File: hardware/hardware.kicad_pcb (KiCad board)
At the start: 2 copper layers, 85.8 x 41.5 mm, 44 parts, among them J1 USB_C_Receptacle_USB2.0_16P, J2 Conn_01x02_Pin, J3 C-OBD-II-16M, J4 Conn_01x06, J5 Conn_01x02_Pin, J6 Conn_01x06, SW3 Reset, SW4 Boot, U1 ESP32-S3-WROOM-1U-N16R8, U2 MCP2515-xSO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

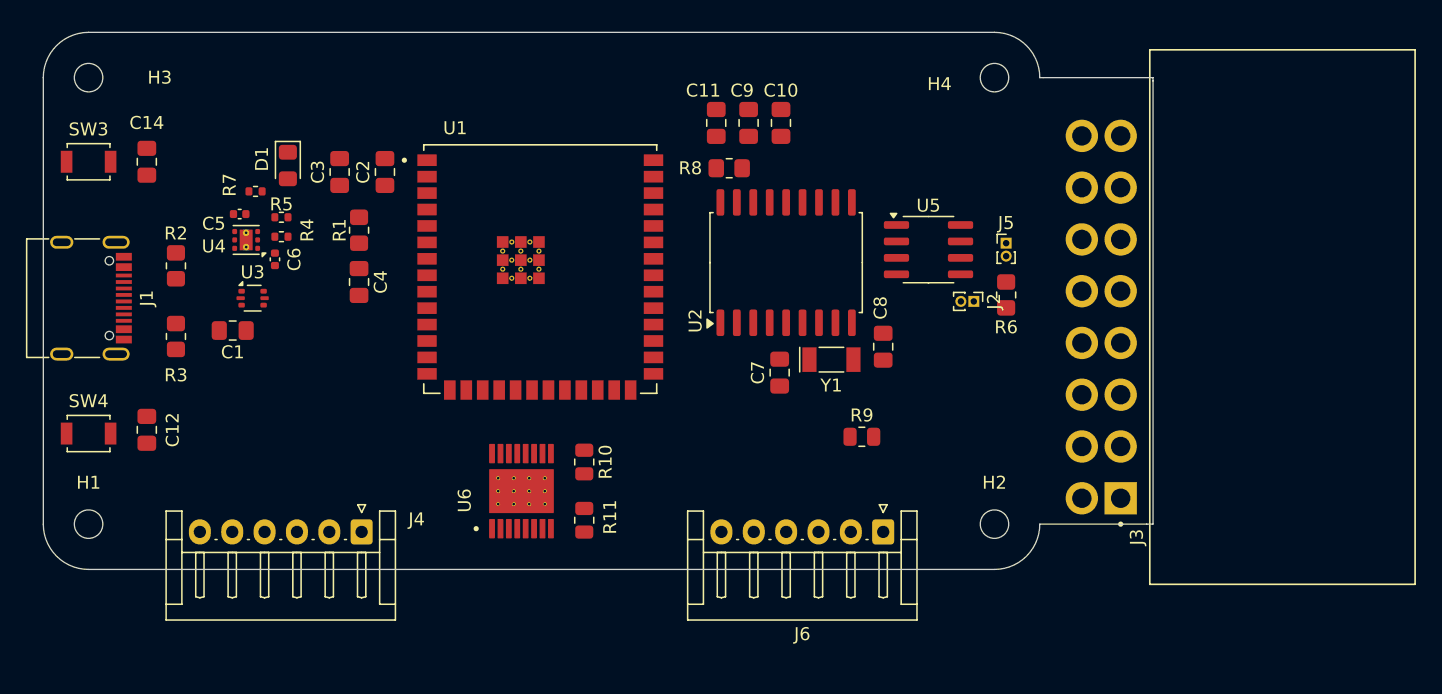
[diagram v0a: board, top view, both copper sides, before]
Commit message: Motor driver and connector
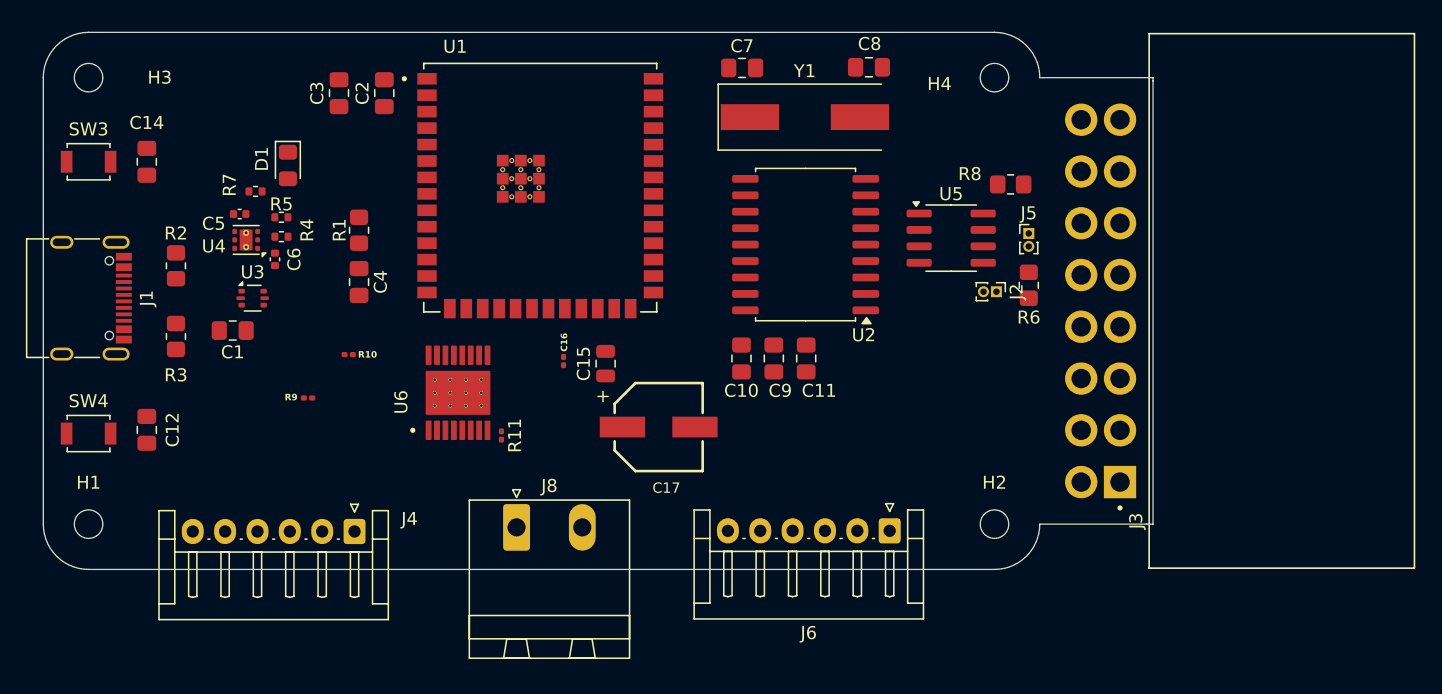
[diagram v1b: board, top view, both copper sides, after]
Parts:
- added C15: 1uF/50V, Capacitor_SMD:C_0805_2012Metric, F.Cu at (90.0, 64.1)
- added C16: 0.1uF, Capacitor_SMD:C_0201_0603Metric, F.Cu at (86.7, 63.9)
- added C17: 47uF/50V, WCAP-ASLI_6.3X7.7:WCAP-ASLI_6.3X7.7_DXL_, F.Cu at (94.0, 69.0)
- added J8: Screw_Terminal_01x02, Connector_Phoenix_MSTB:PhoenixContact_MSTBA_2,5_2-G-5,08_1x02_P5.08mm_Horizontal, F.Cu at (83.1, 76.8)
- R10, R11, R9: footprint Resistor_SMD:R_0805_2012Metric -> Resistor_SMD:R_0201_0603Metric
- Y1: footprint Crystal:Crystal_SMD_MicroCrystal_CC5V-T1A-2Pin_4.1x1.5mm -> Crystal:Crystal_SMD_HC49-SD
- moved R9 42.9 mm to (67.0, 66.8), turned to 180 degrees
- moved C7 23.7 mm to (100.5, 41.2), turned to 0 degrees
- moved R8 21.8 mm to (121.2, 50.2)
- moved C8 21.6 mm to (110.3, 41.2), turned to 0 degrees
- moved R10 20.0 mm to (70.1, 63.4), turned to 0 degrees
- moved C11 19.5 mm to (105.5, 63.7), turned to -90 degrees
- moved Y1 18.9 mm to (105.3, 45.0)
- moved C10 18.5 mm to (100.5, 63.7), turned to -90 degrees
- moved C9 18.3 mm to (103.0, 63.7), turned to -90 degrees
- moved R11 9.16 mm to (81.9, 69.7), turned to -90 degrees
- moved U6 9.04 mm to (78.5, 66.3)
- moved U1 6.29 mm to (84.9, 50.5)
- moved C2 6.09 mm to (72.8, 43.2)
- moved C3 6.09 mm to (69.3, 43.2)
- moved U2 2.05 mm to (105.4, 54.9), turned to 180 degrees
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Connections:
- U1 pad 17: unconnected-(U1-IO9-Pad17) -> /PWM_A1
- U1 pad 18: unconnected-(U1-IO10-Pad18) -> /PWM_A2
- U1 pad 19: /CAN_INT -> /PWM_B1
- U1 pad 20: unconnected-(U1-IO12-Pad20) -> /PWM_B2
- U1 pad 31: unconnected-(U1-IO38-Pad31) -> /CAN_INT
- U1 pad 38: /PWM -> unconnected-(U1-IO2-Pad38)
- U6 pad 10: unconnected-(U6-BIN2-Pad10) -> /PWM_B2
- U6 pad 12: unconnected-(U6-VM-Pad12) -> /V_Motor
- U6 pad 15: unconnected-(U6-AIN2-Pad15) -> /PWM_A2
- U6 pad 16: /PWM -> /PWM_A1
- U6 pad 9: unconnected-(U6-BIN1-Pad9) -> /PWM_B1

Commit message: Added Leds and moved from 2 to 4 layers pcb
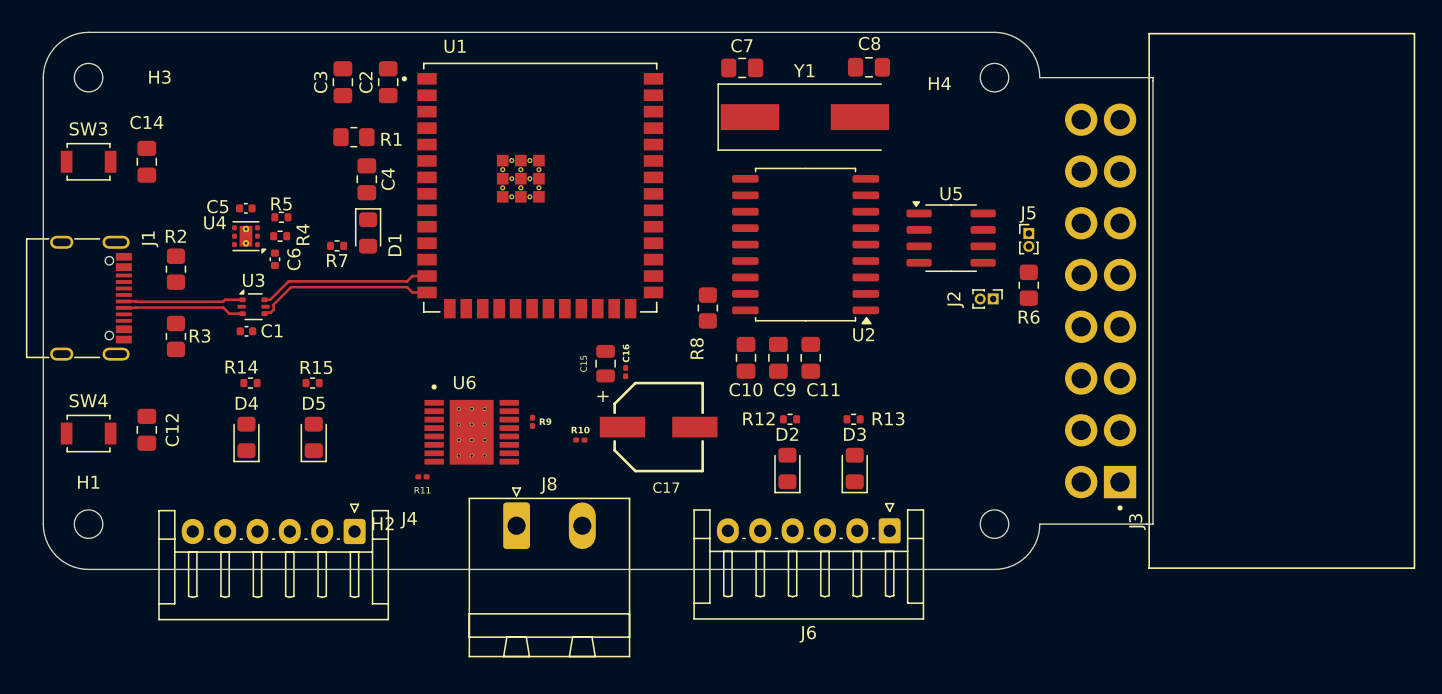
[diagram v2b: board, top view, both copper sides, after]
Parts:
- added D2: LED, LED_SMD:LED_0805_2012Metric_Pad1.15x1.40mm_HandSolder, F.Cu at (104.0, 72.2)
- added D3: LED, LED_SMD:LED_0805_2012Metric_Pad1.15x1.40mm_HandSolder, F.Cu at (109.2, 72.2)
- added D4: LED, LED_SMD:LED_0805_2012Metric_Pad1.15x1.40mm_HandSolder, F.Cu at (62.2, 69.8)
- added D5: LED, LED_SMD:LED_0805_2012Metric_Pad1.15x1.40mm_HandSolder, F.Cu at (67.4, 69.8)
- added R12: 130, Resistor_SMD:R_0402_1005Metric, F.Cu at (104.2, 68.4)
- added R13: 130, Resistor_SMD:R_0402_1005Metric, F.Cu at (109.1, 68.4)
- added R14: 130, Resistor_SMD:R_0402_1005Metric, F.Cu at (62.5, 65.6)
- added R15: 130, Resistor_SMD:R_0402_1005Metric, F.Cu at (67.3, 65.6)
- C1: footprint Capacitor_SMD:C_0805_2012Metric_Pad1.18x1.45mm_HandSolder -> Capacitor_SMD:C_0402_1005Metric
- moved R8 25.3 mm to (97.8, 59.8), turned to -90 degrees
- moved R10 19.1 mm to (88.0, 70.0)
- moved R9 17.4 mm to (84.3, 68.6), turned to -90 degrees
- moved D1 8.10 mm to (71.6, 54.0)
- moved C4 7.96 mm to (71.5, 49.9)
- moved R7 7.58 mm to (69.2, 55.0)
- moved R1 7.20 mm to (70.5, 46.6), turned to 0 degrees
- moved R11 6.89 mm to (75.8, 72.8), turned to 180 degrees
- moved C16 4.87 mm to (91.5, 64.8)
- moved U6 3.23 mm to (79.6, 69.4), turned to 0 degrees
- moved C1 1.06 mm to (62.2, 61.6)
- moved C2 0.90 mm to (73.2, 42.4)
- moved C3 0.90 mm to (69.7, 42.4)
- moved U3 0.66 mm to (62.8, 59.7)
- moved C5 0.65 mm to (62.1, 52.1)
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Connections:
- J4 pad 2: /EncoderA+ -> /3.3V
- J4 pad 5: /EncoderA- -> GND
- J6 pad 2: /EncoderB+ -> /3.3V
- J6 pad 5: /EncoderB- -> GND
- U1 pad 13: /GPIO19 -> /D-
- U1 pad 14: /GPIO20 -> /D+
- U1 pad 19: /PWM_B1 -> /PWM_B2
- U1 pad 20: /PWM_B2 -> /PWM_B1
- U1 pad 21: unconnected-(U1-IO13-Pad21) -> /PulseB_01
- U1 pad 22: /Pulse_01 -> /PulseB_02
- U1 pad 31: /CAN_INT -> /CS
- U1 pad 32: /SCLK -> /MISO
- U1 pad 34: /MISO -> /SCLK
- U1 pad 35: /CS -> /CAN_INT
- U1 pad 8: /Pulse_02 -> /PulseA_02
- U1 pad 9: unconnected-(U1-IO16-Pad9) -> /PulseA_01
- U3 pad 4: /GPIO20 -> /D+
- U3 pad 6: /GPIO19 -> /D-
- U6 pad 10: /PWM_B2 -> unconnected-(U6-BIN2-Pad10)
- U6 pad 15: /PWM_A2 -> unconnected-(U6-AIN2-Pad15)
- U6 pad 16: /PWM_A1 -> unconnected-(U6-AIN1-Pad16)
- U6 pad 9: /PWM_B1 -> unconnected-(U6-BIN1-Pad9)
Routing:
- net /D+: track 0.00 -> 23.2 mm
- net /D-: track 0.00 -> 22.6 mm
- added copper zone on In1.Cu, net GND
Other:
- copper layers 2 -> 4

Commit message: Changed motor driver IC from DRV8411 to DRV8871 PCB updated as well added manufacture values in schematics
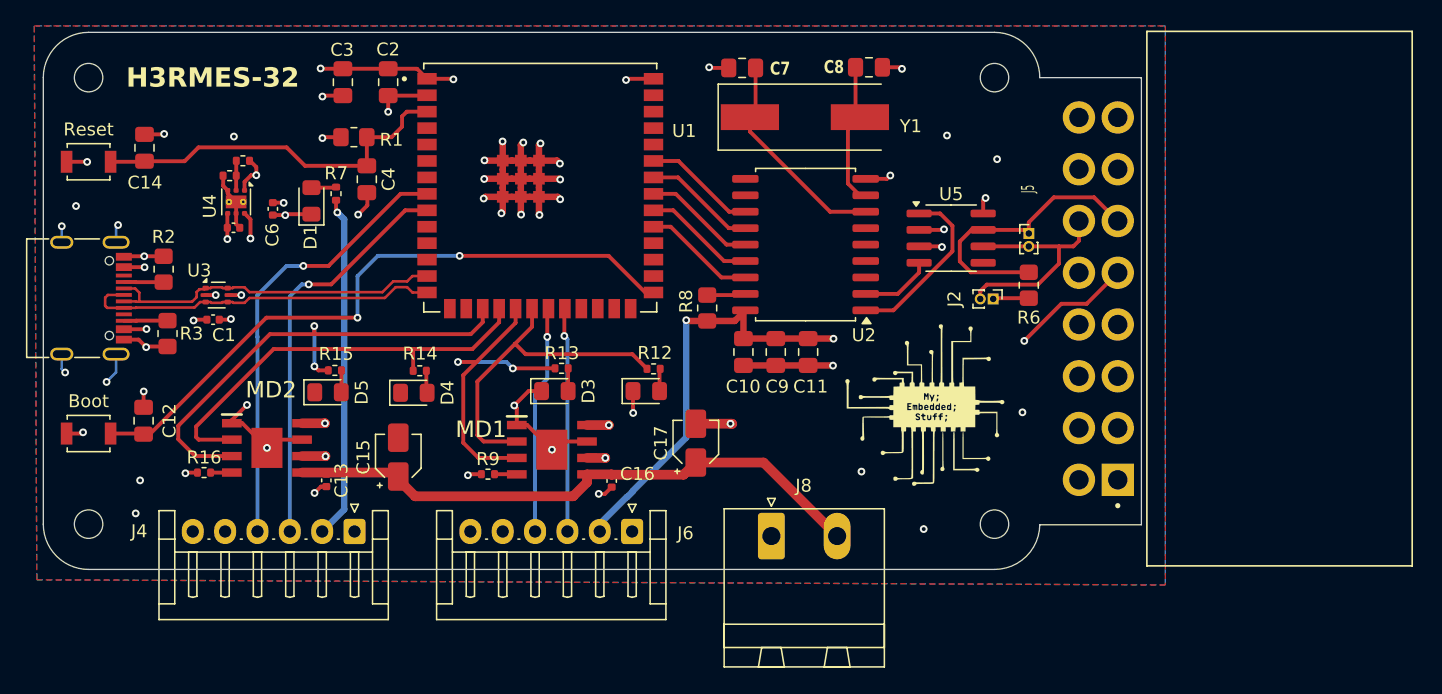
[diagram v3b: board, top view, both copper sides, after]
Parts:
- removed R10: R, Resistor_SMD:R_0201_0603Metric
- removed R11: 10K, Resistor_SMD:R_0201_0603Metric
- removed U6: DRV8411APWPR, DRV8411APWPR:IC_DRV8411APWPR
- added C13: 0.1uF, Capacitor_SMD:C_0402_1005Metric, F.Cu at (68.4, 73.1)
- added G***: LOGO, LOGO, F.Cu at (114.6, 67.6)
- added MD1: DRV8871DDARQ1, DRV8871DDARQ1:SOIC127P600X170-9N, F.Cu at (85.8, 70.8)
- added MD2: DRV8871DDARQ1, DRV8871DDARQ1:SOIC127P600X170-9N, F.Cu at (63.8, 70.6)
- added R16: 32K, Resistor_SMD:R_0402_1005Metric, F.Cu at (58.9, 72.5)
- C15: value 1uF/50V -> 47uF/50V; footprint Capacitor_SMD:C_0805_2012Metric -> Capacitor_SMD:CP_Elec_3x5.4
- C16: footprint Capacitor_SMD:C_0201_0603Metric -> Capacitor_SMD:C_0402_1005Metric
- C17: footprint WCAP-ASLI_6.3X7.7:WCAP-ASLI_6.3X7.7_DXL_ -> Capacitor_SMD:CP_Elec_3x5.4
- R12, R13, R14, R15, R7: value 130 -> 1.5K
- R9: value R -> 32K; footprint Resistor_SMD:R_0201_0603Metric -> Resistor_SMD:R_0402_1005Metric
- moved D3 23.9 mm to (86.0, 66.2), turned to 0 degrees
- moved R13 22.9 mm to (86.5, 64.5)
- moved J6 19.9 mm to (92.0, 77.1)
- moved J8 19.7 mm to (102.8, 77.4)
- moved C15 17.6 mm to (73.9, 71.3)
- moved D4 13.4 mm to (75.1, 66.3), turned to 0 degrees
- moved R14 13.1 mm to (75.6, 64.7), turned to 180 degrees
- moved D2 12.4 mm to (93.1, 66.2), turned to 0 degrees
- moved R12 11.2 mm to (93.7, 64.5)
- moved C16 8.48 mm to (90.4, 73.2), turned to -90 degrees
- moved R4 6.50 mm to (61.9, 48.4)
- moved R9 5.31 mm to (80.9, 72.6), turned to 0 degrees
- moved R5 5.13 mm to (60.9, 49.6)
- moved D1 5.03 mm to (67.2, 51.5), turned to 90 degrees
- moved R7 4.04 mm to (69.1, 51.0), turned to -90 degrees
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- renumbered SW4 to Boot, SW3 to Reset
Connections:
- J4 pad 1: /MotorA+ -> /MotorA-
- J4 pad 6: /MotorA- -> /MotorA+
- J6 pad 1: /MotorB+ -> /MotorB-
- J6 pad 6: /MotorB- -> /MotorB+
- R9 pad 1: Net-(U6-AIPROPI) -> GND
- R9 pad 2: GND -> Net-(IC1-ILIM)
- U1 pad 19: /PWM_B2 -> /PWM_B1
- U1 pad 20: /PWM_B1 -> /PWM_B2
- U1 pad 21: /PulseB_01 -> /PulseB_02
- U1 pad 22: /PulseB_02 -> /PulseB_01
- U4 pad 7: unconnected-(U4-PAD-Pad7)_2 -> GND
- U5 pad 1: /RX_CAN -> /TX_CAN
- U5 pad 4: /TX_CAN -> /RX_CAN
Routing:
- net GND: track 0.00 -> 132.1 mm, vias 0 -> 55
- net /3.3V: track 0.00 -> 72.9 mm, vias 0 -> 9
- net /GPIO0: track 0.00 -> 50.9 mm, vias 0 -> 2
- net /V_Motor: track 0.00 -> 45.9 mm
- net /PWM_A1: track 0.00 -> 38.6 mm, vias 0 -> 2
- net /PulseA_02: track 0.00 -> 35.4 mm, vias 0 -> 1
- net /PWM_A2: track 0.00 -> 33.1 mm
- net /PulseA_01: track 0.00 -> 31.5 mm, vias 0 -> 1
- net /Enable: track 0.00 -> 29.0 mm
- net /PWM_B1: track 0.00 -> 25.8 mm, vias 0 -> 2
- net /PWM_B2: track 0.00 -> 25.8 mm
- net /CANH: track 0.00 -> 22.3 mm
- net /CANL: track 0.00 -> 18.0 mm
- net /PulseB_02: track 0.00 -> 17.6 mm, vias 0 -> 1
- net /PulseB_01: track 0.00 -> 17.3 mm, vias 0 -> 1
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- added copper zone on In2.Cu, net /3.3V
- added copper zone on In2.Cu, net /5V
- added copper zone on In2.Cu, net /MotorA+
- added copper zone on In2.Cu, net /MotorA-
- added copper zone on In2.Cu, net /MotorB+
- added copper zone on In2.Cu, net /MotorB-
- added copper zone on B.Cu, net GND
- added copper zone on F.Cu, net GND
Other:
- board size 85.8 x 41.5 mm -> 84.8 x 41.5 mm
- board text added: "H3RMES-32"

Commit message: version 1
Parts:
- C13, C16: value 0.1uF -> CL05B104KO5NNNC
- C15, C17: value 47uF/50V -> RVT47UF35V67RV0039; footprint Capacitor_SMD:CP_Elec_3x5.4 -> Capacitor_SMD:CP_Elec_6.3x5.4
- C6: value 2.2uF -> CL05A225MQ5NSNC
- J1: value USB_C_Receptacle_USB2.0_16P -> TYPE-C-31-M-12
- R12, R13, R14, R15, R7: value 1.5K -> 0402WGF1501TCE
- R16, R9: value 32K -> 0402WGJ0303TCE
- R4: value 499K -> 0402WGJ0513TCE
- R5: value 160K -> 0402WGJ0163TCE
- SW3: renamed from Reset; value Reset -> GT-TC032A-H015-L1
- SW4: renamed from Boot; value Boot -> GT-TC032A-H015-L1
- U4: value TLV76701DRVx -> TLV76701DRVR
- Y1: value 8Mhz -> X49SM8MSD2SC
- moved D2 3.12 mm to (90.0, 66.2)
- moved R12 3.11 mm to (90.5, 64.4)
- moved D3 2.24 mm to (83.8, 66.3)
- moved R13 2.23 mm to (84.3, 64.5)
- moved C6 1.21 mm to (63.5, 51.2)
- moved D4 1.19 mm to (74.8, 65.2)
- moved C15 1.16 mm to (75.1, 71.2)
- moved R14 1.11 mm to (75.3, 63.6)
- moved J4 0.98 mm to (70.5, 78.0)
- moved J6 0.98 mm to (92.0, 78.0)
- moved C17 0.87 mm to (97.0, 69.4)
- renumbered MD1 to IC1, MD2 to IC2
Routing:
- net GND: track 132.1 -> 135.3 mm, vias 55 -> 59
- net /PWM_B2: track 25.8 -> 23.0 mm
- net /3.3V: track 72.9 -> 75.5 mm, vias 9 -> 8
- net /PWM_B1: track 25.8 -> 23.6 mm
- net /PulseB_01: track 17.3 -> 19.3 mm
- net /PulseA_01: track 31.5 -> 32.5 mm
- net /PulseB_02: track 17.6 -> 18.6 mm
- net /PWM_A2: track 33.1 -> 32.4 mm
- net /V_Motor: track 45.9 -> 45.3 mm
